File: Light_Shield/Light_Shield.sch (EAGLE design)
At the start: 35 parts, among them U1 ARDUINO_SHIELDLABEL

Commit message: Updates Light Shield schematic to most recent version. Renames schematic to Light_Shield.sch Adds Victor's name in the designer block.
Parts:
- added 1, 2, 200, 2K1, 2K2, 2K7: (no value), SparkFun-Resistors:RESISTOR0603
- added R12, R13, R14, R15, R16, R17: 200, SparkFun-Resistors:RESISTOR0603
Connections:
- new net N$11: R17.2, T5.B
- new net N$13: R16.2, T4.B
- new net N$14: R15.2, T6.B
- new net N$15: R14.2, T17.B
- new net N$16: R13.2, T15.B
- new net N$17: R12.2, T16.B
- new net N$18: 1.1, 2K1.1, T2.B
- new net N$19: 2.1, 2K2.1, T3.B
- new net N$9: 200.1, 2K7.1, T1.B
- net 12V: now also 1.2, 2.2, 200.2
- net 1S1_CTRL: no longer T16.B
- net 1S1_OUT: now also R12.1
- net 1S2_CTRL: no longer T15.B
- net 1S2_OUT: now also R13.1
- net 1S3_CTRL: no longer T17.B
- net 1S3_OUT: now also R14.1
- net 2S1_CTRL: no longer T5.B
- net 2S1_OUT: now also R17.1
- net 2S2_CTRL: no longer T4.B
- net 2S2_OUT: now also R16.1
- net 2S3_CTRL: no longer T6.B
- net 2S3_OUT: now also R15.1
- net BLUE_CTRL: now also 2K1.2; no longer T3.B
- net BLUE_OUT: now also T2.C; no longer T3.C
- net GREEN_CTRL: now also 2K2.2; no longer T2.B
- net GREEN_OUT: now also T3.C; no longer T2.C
- net RED_CTRL: now also 2K7.2; no longer T1.B
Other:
- note added: "Victor Ying"
- moved on the sheet: ARDUINO_ON, C1, D3, JP1, JP2, POWER_ON, Q1, R1, R10, R11, R2, R3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

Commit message: updates schematic to match board file
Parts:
- removed 1, 2, 200, 2K1, 2K2, 2K7: (no value), SparkFun-Resistors:RESISTOR0603
- added JP3, JP4: M02POLAR, SparkFun-Connectors:M02POLAR
- added R18, R19, R20: 2700, SparkFun-Resistors:RESISTOR0603
- added R21, R22, R23: 200, SparkFun-Resistors:RESISTOR0603
- R10, R11: value (none) -> 2700
- R3: value 2200 -> 200
- R5, R6, R7, R8, R9: value (none) -> 200
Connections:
- net 12V: now also D3.C, JP4.1, R11.2, R21.2, R22.2, R23.2; no longer 1.2, 2.2, 200.2, Q1.C, R5.2
- net BLUE_CTRL: now also R19.2; no longer 2K1.2
- net GND: now also Q1.E; no longer R11.1
- net GREEN_CTRL: now also R20.2; no longer 2K2.2
- net N$18: now also R19.1, R22.1; no longer 1.1, 2K1.1
- net N$19: now also R20.1, R23.1; no longer 2.1, 2K2.1
- net N$6: now also Q1.C, R11.1; no longer Q1.E, R11.2
- net N$7: now also D3.A, R5.2; no longer D3.C, R5.1
- net N$8: now also R5.1; no longer D3.A
- net N$9: now also R18.1, R21.1; no longer 200.1, 2K7.1
- net RED_CTRL: now also R18.2; no longer 2K7.2
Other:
- note removed: "Victor Ying"
- moved on the sheet: ARDUINO_ON, C1, D3, JP1, JP2, POWER_ON, Q1, R1, R10, R11, R12, R13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

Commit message: New Light Shield Schematic and Board
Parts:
- R2: value 300 -> 200
- T17, T6: device transistor:-NPN-TO220 -> transistor:-NPN-TO220V
- renumbered U$1 to Q2
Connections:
- net 1S1_CTRL: now also R12.1
- net 1S1_OUT: now also T16.C; no longer R12.1, T16.E
- net 1S2_CTRL: now also R13.1
- net 1S2_OUT: now also T15.C; no longer R13.1, T15.E
- net 1S3_CTRL: now also R14.1
- net 1S3_OUT: now also T17.C; no longer R14.1, T17.E, T6.E
- net 24V: now also JP3.1
- net 2S1_CTRL: now also R17.1
- net 2S1_OUT: now also T5.C; no longer R17.1, T5.E
- net 2S2_CTRL: now also R16.1
- net 2S2_OUT: now also T4.C; no longer R16.1, T4.E
- net 2S3_CTRL: now also R15.1
- net 2S3_OUT: now also T6.C; no longer R15.1
- net GND: now also T15.E, T16.E, T17.E, T4.E, T5.E, T6.E; no longer T15.C, T16.C, T17.C, T4.C, T5.C, T6.C

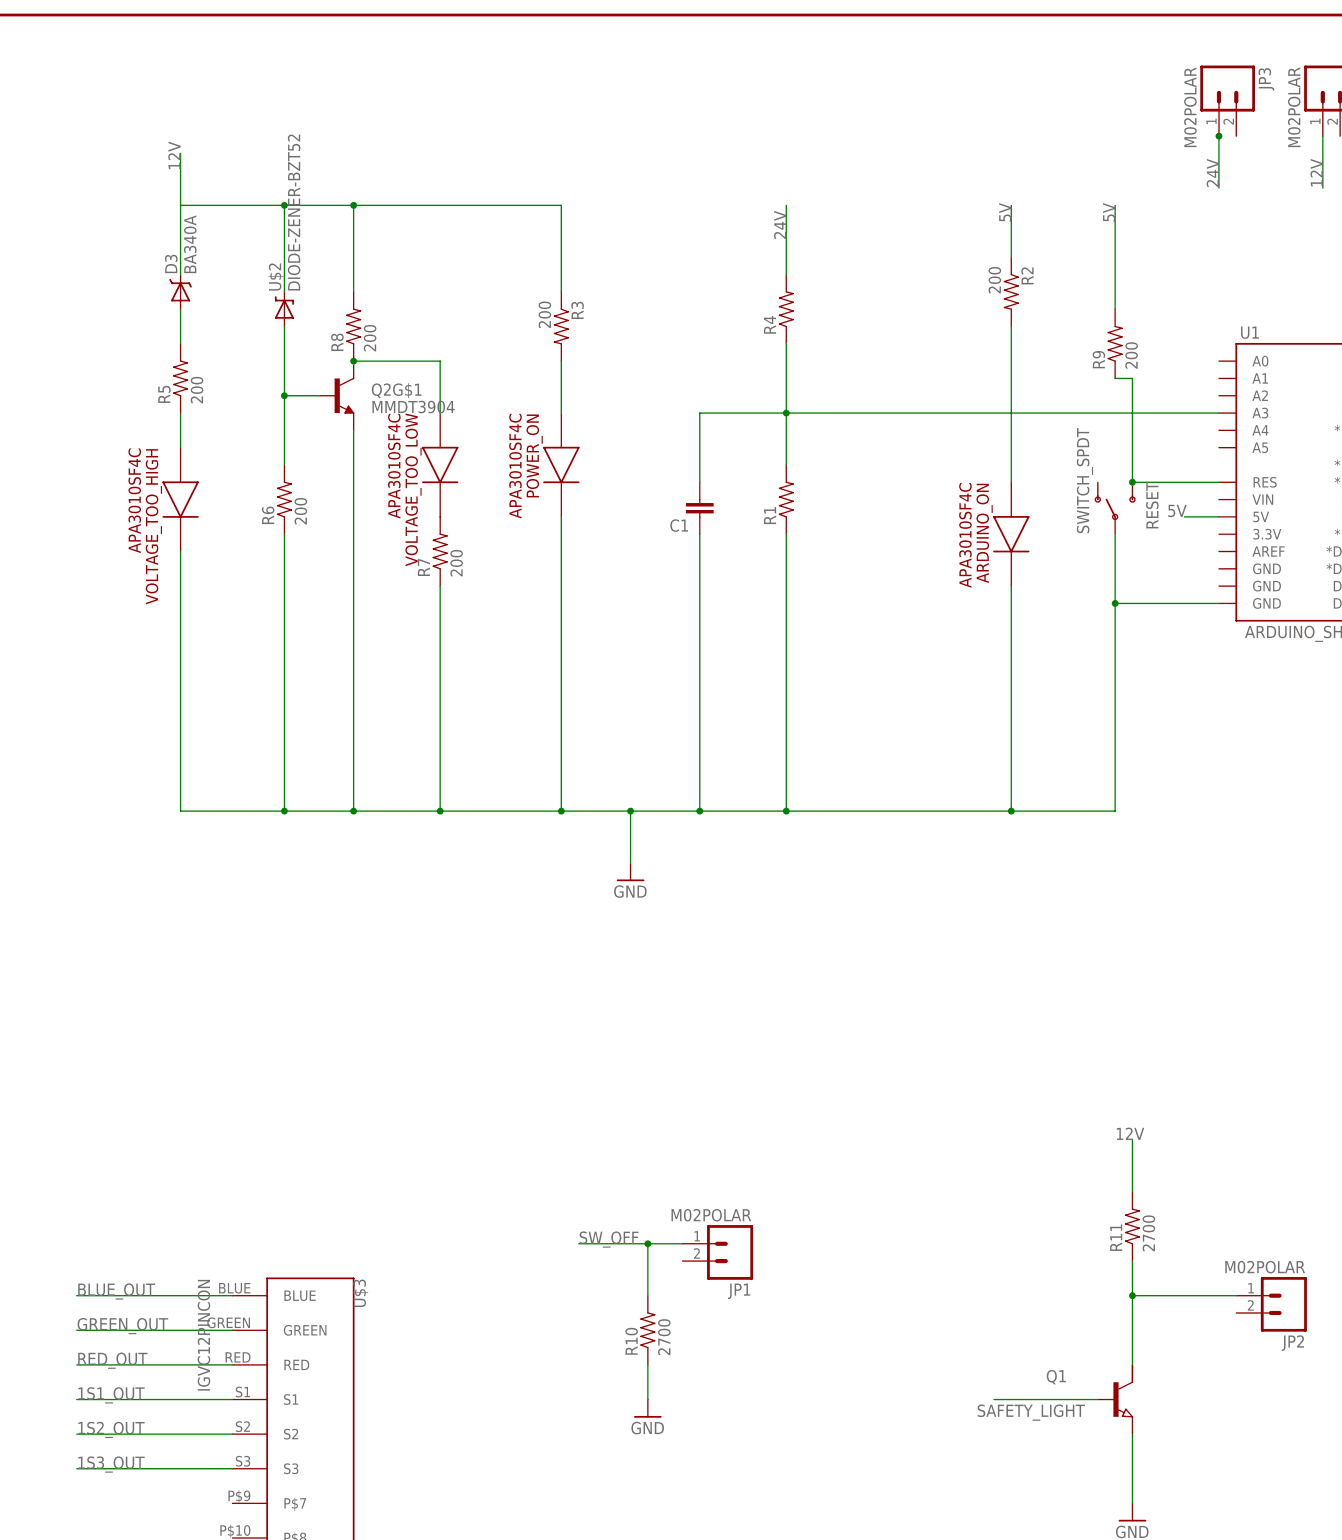
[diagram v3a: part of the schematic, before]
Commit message: Chaged the Q1 and Q1 transistors, changed switch to tactile switch version
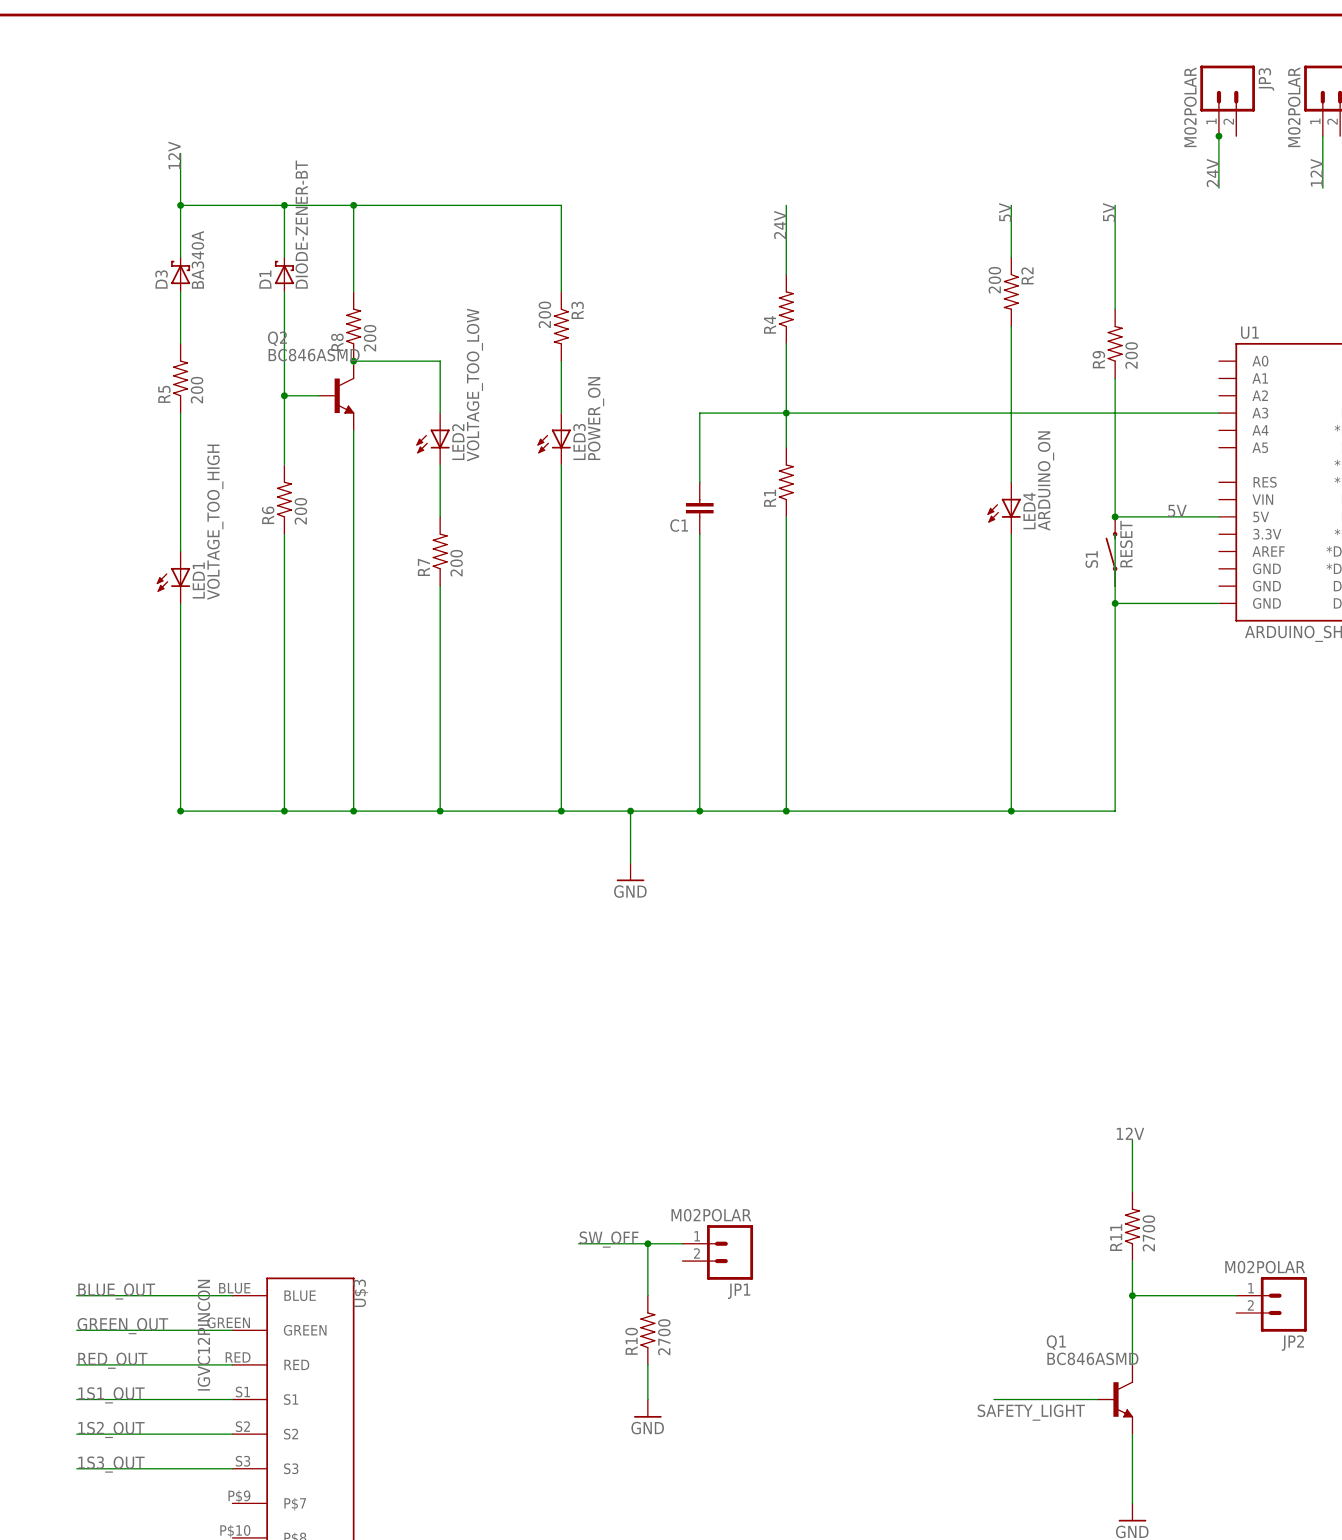
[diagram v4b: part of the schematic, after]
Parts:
- removed ARDUINO_ON, POWER_ON, VOLTAGE_TOO_HIGH, VOLTAGE_TOO_LOW: APA3010SF4C, SparkFun-LED:APA3010SF4C
- removed RESET: SWITCH_SPDT, SparkFun-Electromechanical:SWITCH_SPDT
- removed U$2: DIODE-ZENER-BZT52, SparkFun-DiscreteSemi:DIODE-ZENER-BZT52
- added D1: DIODE-ZENER-BT, diode:SMF5.0AT1
- added LED1: VOLTAGE_TOO_HIGH, led:LEDSML0603
- added LED2: VOLTAGE_TOO_LOW, led:LEDSML0603
- added LED3: POWER_ON, led:LEDSML0603
- added LED4: ARDUINO_ON, led:LEDSML0603
- added S1: RESET, SparkFun-Electromechanical:SWITCH-MOMENTARY-2PTH
- D3: device SparkFun-DiscreteSemi:B340A -> diode:SMF5.0AT1
- Q1: value (none) -> BC846ASMD; device semicon-smd-ipc:NPN-TRANSISTIOR-2COLSOT143 -> transistor-npn:BC846ASMD
- Q2: value MMDT3904 -> BC846ASMD; device SparkFun-DiscreteSemi:MMDT3904 -> transistor-npn:BC846ASMD
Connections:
- removed net N$12: R9.1, RESET.S, U1.RES
- net 12V: now also D1.C; no longer U$2.C
- net 5V: now also R9.1, S1.2
- net GND: now also LED1.C, LED3.C, LED4.C, Q2.E, S1.1; no longer ARDUINO_ON.2, POWER_ON.2, Q2G$1.E, RESET.P, VOLTAGE_TOO_HIGH.2
- net N$10: now also LED2.C; no longer VOLTAGE_TOO_LOW.2
- net N$2: now also LED3.A; no longer POWER_ON.1
- net N$3: now also LED2.A, Q2.C; no longer Q2G$1.C, VOLTAGE_TOO_LOW.1
- net N$4: now also D1.A, Q2.B; no longer Q2G$1.B, U$2.A
- net N$5: now also LED4.A; no longer ARDUINO_ON.1
- net N$8: now also LED1.A; no longer VOLTAGE_TOO_HIGH.1
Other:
- moved on the sheet: R1

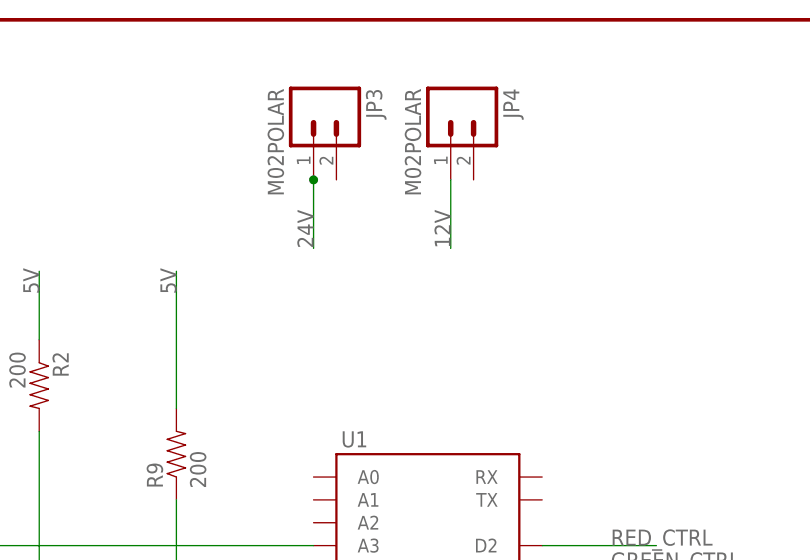
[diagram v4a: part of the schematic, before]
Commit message: Redesigned configuration of board
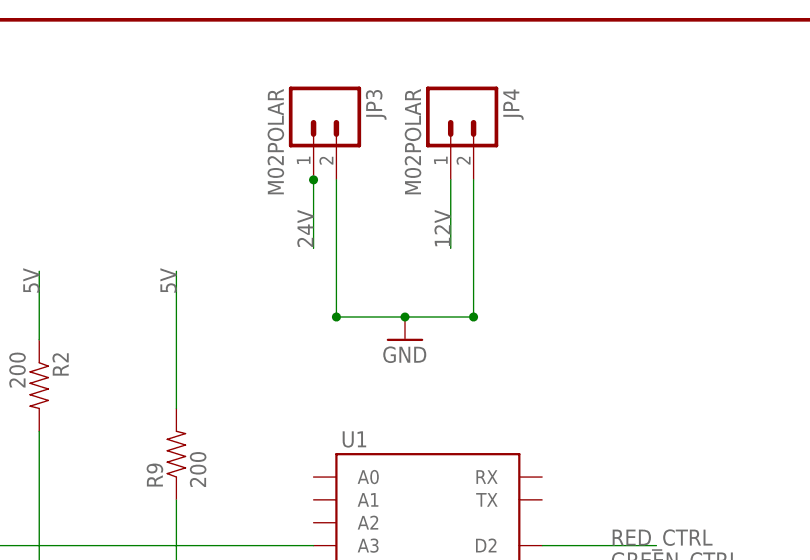
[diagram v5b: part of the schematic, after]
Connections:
- net GND: now also JP3.2, JP4.2
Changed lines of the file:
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@@
 <part name="LED4" library="led" deviceset="LED" device="SML0603" value="ARDUINO_ON"/>
 <part name="S1" library="SparkFun-Electromechanical" deviceset="SWITCH-MOMENTARY-2" device="PTH" value="RESET"/>
+<part name="GND4" library="SparkFun-Aesthetics" deviceset="GND" device=""/>
 </parts>
 <sheets>
@@
 <instance part="LED4" gate="G$1" x="353.06" y="312.42"/>
 <instance part="S1" gate="G$1" x="368.3" y="304.8" rot="R90"/>
+<instance part="GND4" gate="1" x="393.7" y="347.98"/>
 </instances>
 <busses>
@@
 <pinref part="T6" gate="G$1" pin="E"/>
 </segment>
+<segment>
+<pinref part="JP3" gate="G$1" pin="2"/>
+<wire x1="386.08" y1="365.76" x2="386.08" y2="350.52" width="0.1524" layer="91"/>
+<pinref part="GND4" gate="1" pin="GND"/>
+<wire x1="386.08" y1="350.52" x2="393.7" y2="350.52" width="0.1524" layer="91"/>
+<pinref part="JP4" gate="G$1" pin="2"/>
+<wire x1="401.32" y1="365.76" x2="401.32" y2="350.52" width="0.1524" layer="91"/>
+<wire x1="393.7" y1="350.52" x2="401.32" y2="350.52" width="0.1524" layer="91"/>
+<junction x="386.08" y="350.52"/>
+<junction x="393.7" y="350.52"/>
+<junction x="401.32" y="350.52"/>
+</segment>
 </net>

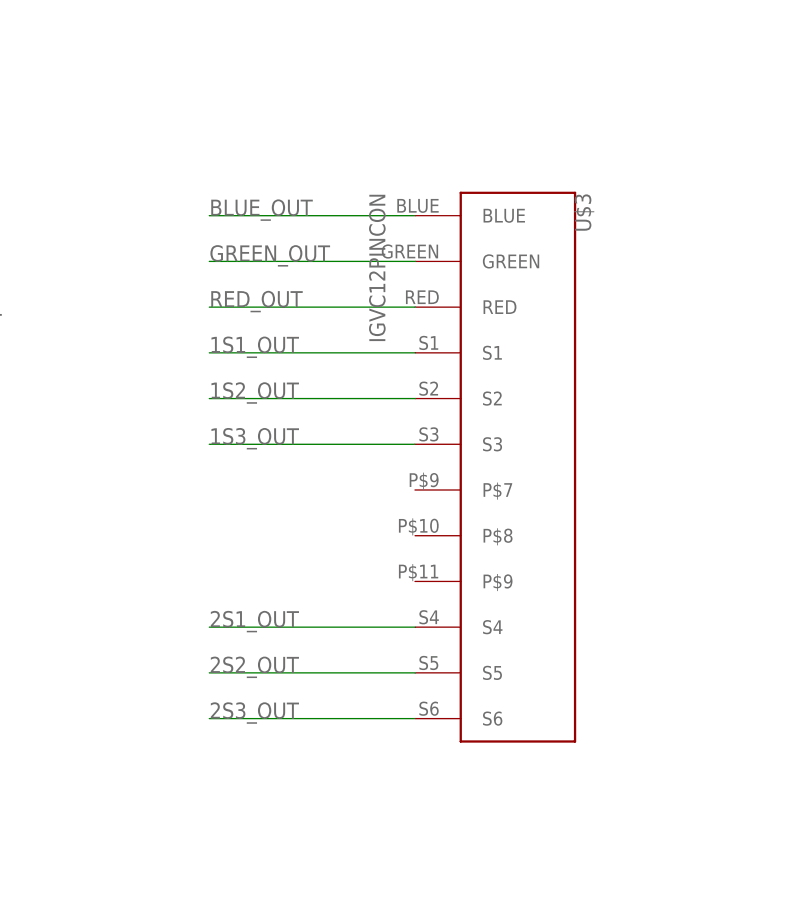
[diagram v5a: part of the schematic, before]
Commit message: Updated version of light shield with further placement optimizations
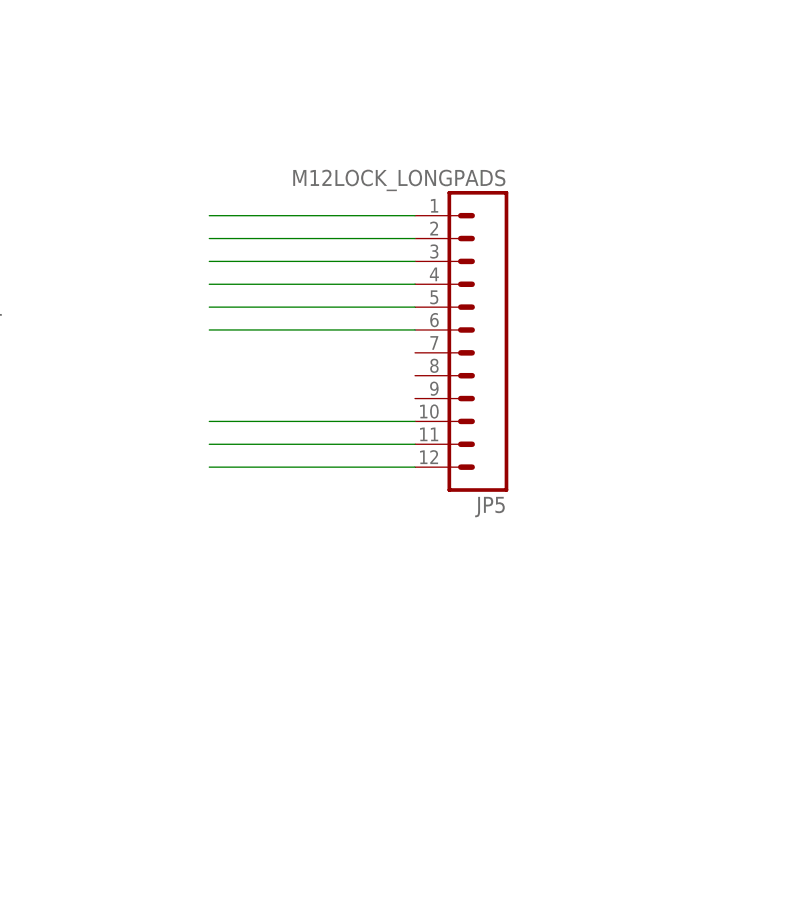
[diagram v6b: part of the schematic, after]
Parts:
- removed U$3: IGVC12PINCON, IGVC12PinCon:IGVC12PINCON
- added JP5: M12LOCK_LONGPADS, SparkFun-Connectors:M12LOCK_LONGPADS
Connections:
- net 1S1_OUT: now also JP5.4; no longer U$3.S1
- net 1S2_OUT: now also JP5.5; no longer U$3.S2
- net 1S3_OUT: now also JP5.6; no longer U$3.S3
- net 2S1_OUT: now also JP5.10; no longer U$3.S4
- net 2S2_OUT: now also JP5.11; no longer U$3.S5
- net 2S3_OUT: now also JP5.12; no longer U$3.S6
- net BLUE_OUT: now also JP5.1; no longer U$3.BLUE
- net GREEN_OUT: now also JP5.2; no longer U$3.GREEN
- net RED_OUT: now also JP5.3; no longer U$3.RED
